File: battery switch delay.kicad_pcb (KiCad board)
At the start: 2 copper layers, 35.5 x 56 mm, 15 parts, among them J1 Conn_01x04, K2 G6E, Q1 2N3904, U2 LT1129-5.0_SOT223

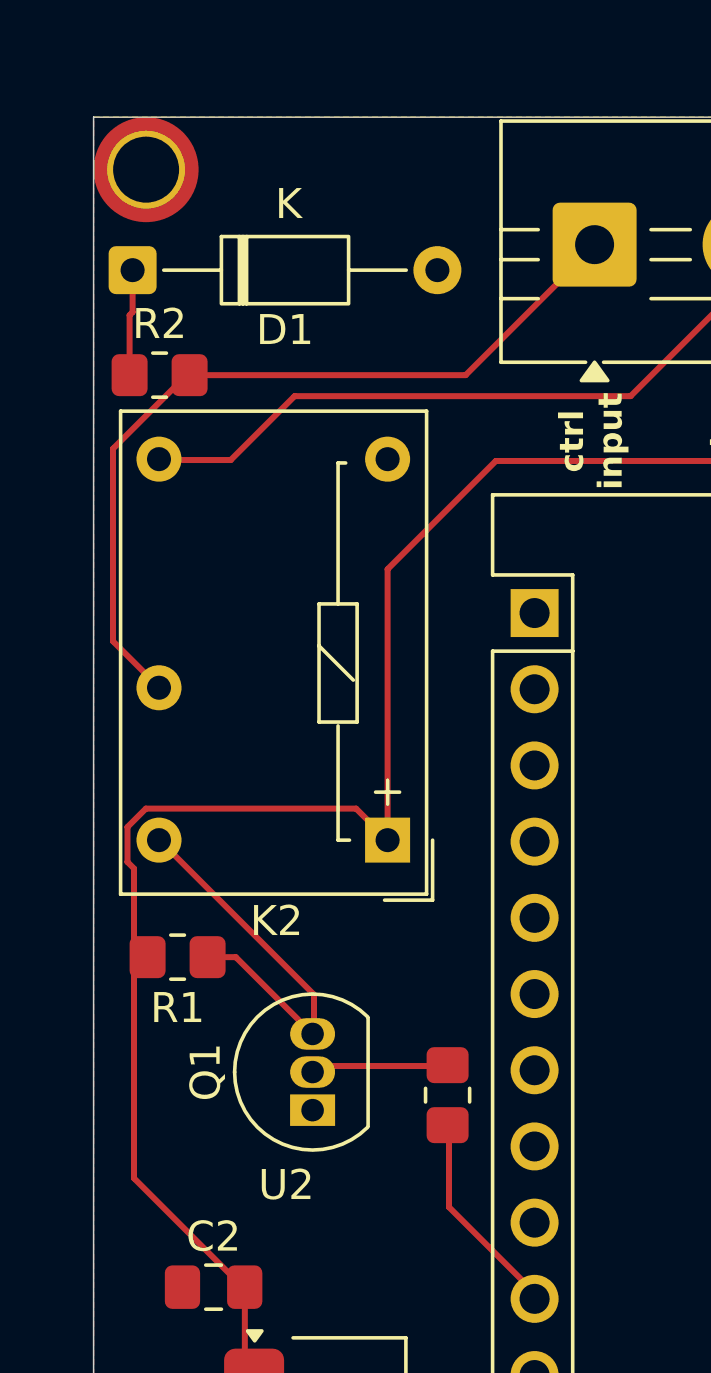
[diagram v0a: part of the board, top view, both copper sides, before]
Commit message: got the transistor the correct footprint hopefully
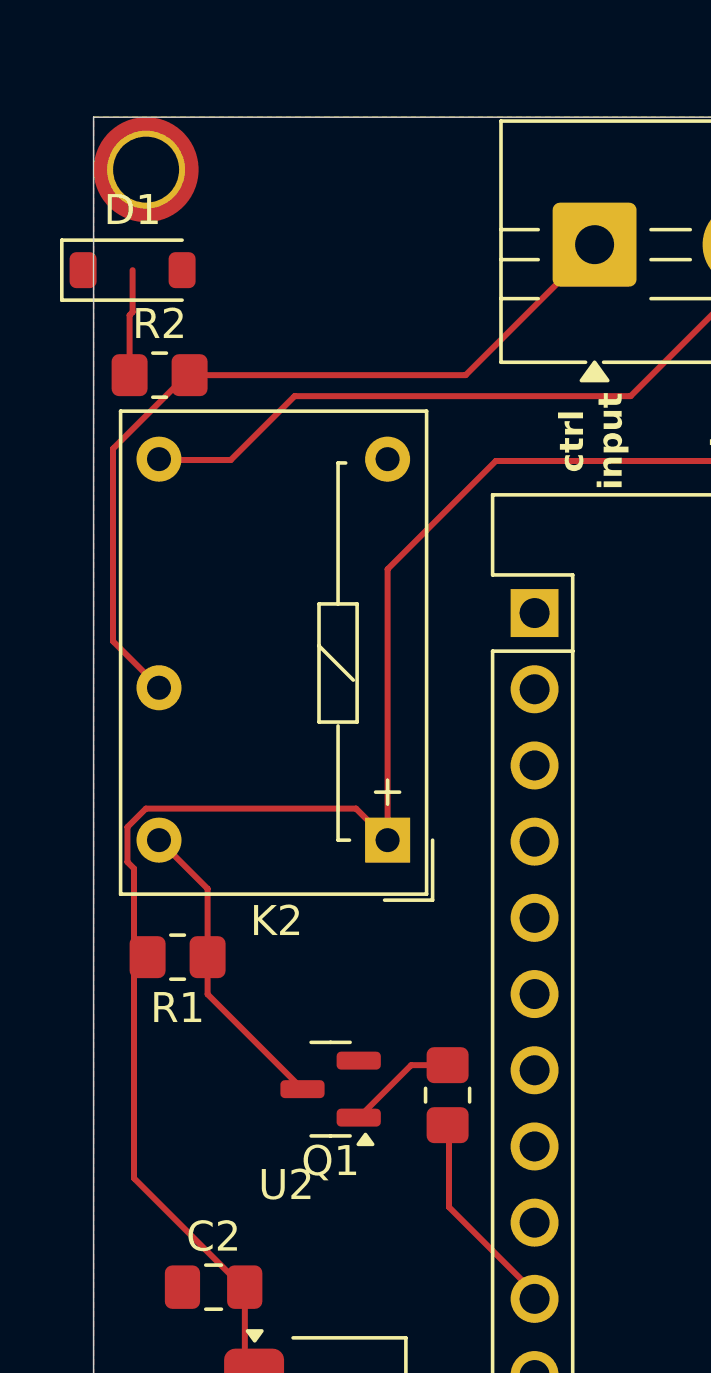
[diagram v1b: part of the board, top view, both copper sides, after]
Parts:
- D1: value ZPDxx -> 4.7v-5.1v zener diode; footprint Diode_THT:D_DO-35_SOD27_P10.16mm_Horizontal -> Diode_SMD:D_SOD-123
- J1: value Conn_01x04 -> 5mm pitch 4 position screw terminal block
- K2: value G6E -> G6E-134P-US
- Q1: value 2N3904 -> Q_NPN; footprint Package_TO_SOT_THT:TO-92_Inline -> Package_TO_SOT_SMD:SOT-23
- U2: value LT1129-5.0_SOT223 -> MIC2920A-12WS-TR_SOT223
- moved Q1 0.92 mm to (116.9, 88.9), turned to 180 degrees
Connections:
- Q1 pad 1: GND -> Net-(Q1-B)
- Q1 pad 2: Net-(Q1-B) -> GND
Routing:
- net Net-(Q1-C): track 13.2 -> 10.3 mm
- net Net-(Q1-B): track 5.14 -> 3.69 mm

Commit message: shuffling things around
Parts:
- moved D1 8.61 mm to (118.9, 61.3), turned to -90 degrees
- moved R3 5.56 mm to (118.0, 93.9), turned to 0 degrees
- moved R2 4.98 mm to (115.1, 62.0), turned to 90 degrees
- moved J1 1.00 mm to (126.7, 60.8)
- moved Q1 0.51 mm to (117.0, 88.4)
- moved R1 0.10 mm to (111.8, 84.6)
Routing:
- net ctrl: track 27.4 -> 30.0 mm
- net Net-(Q1-B): track 3.69 -> 5.52 mm
- net +12V: track 65.0 -> 66.7 mm
- net Net-(A1-D2): track 3.54 -> 5.06 mm
- net Net-(A1-D7): track 7.06 -> 5.60 mm
- net to switch: track 22.9 -> 23.5 mm

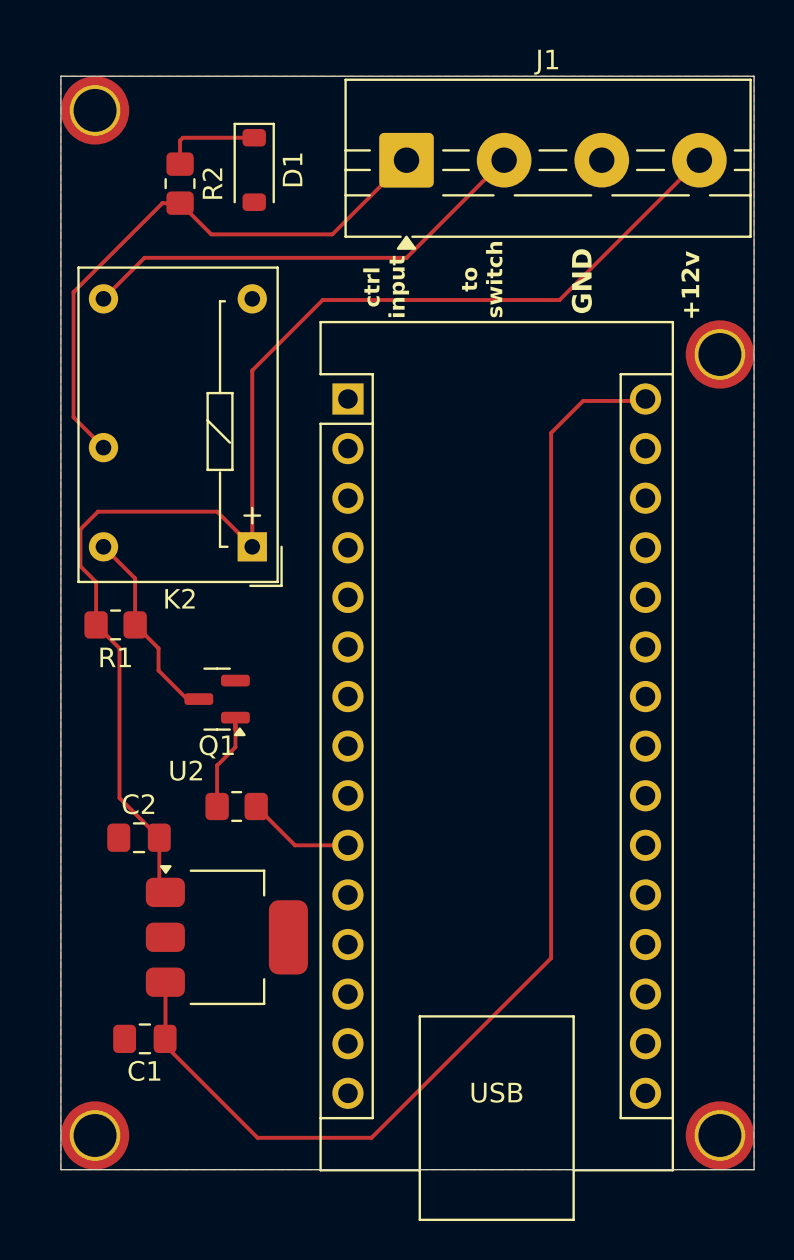
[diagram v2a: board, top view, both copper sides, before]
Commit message: did more board layout and actualy have all nets connected. looking at drc so i can be sure
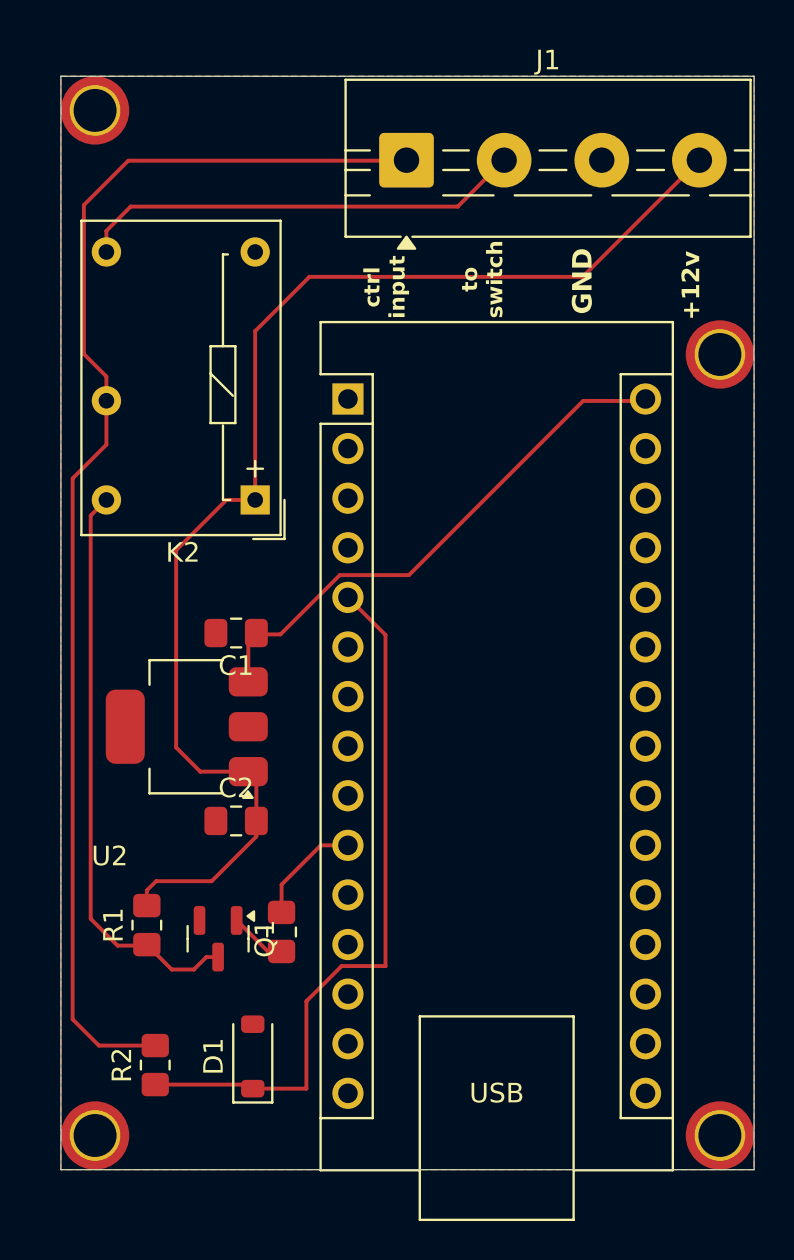
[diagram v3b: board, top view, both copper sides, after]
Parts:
- moved D1 45.4 mm to (118.8, 106.7), turned to 90 degrees
- moved R2 45.2 mm to (113.8, 107.1), turned to -90 degrees
- moved C1 21.3 mm to (118.0, 85.0)
- moved R1 15.5 mm to (113.4, 100.0), turned to -90 degrees
- moved Q1 12.3 mm to (117.0, 100.7), turned to -90 degrees
- moved U2 11.0 mm to (115.4, 89.8), turned to 180 degrees
- moved R3 6.82 mm to (120.3, 100.3), turned to 90 degrees
- moved C2 5.05 mm to (118.0, 94.6)
- moved K2 2.40 mm to (119.0, 78.2)
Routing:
- net ctrl: track 30.0 -> 65.2 mm
- net Net-(A1-VIN): track 61.4 -> 28.6 mm
- net Net-(A1-D2): track 5.06 -> 36.9 mm
- net Net-(Q1-C): track 10.2 -> 30.3 mm
- net Net-(Q1-B): track 5.52 -> 2.96 mm
- net +12V: track 66.7 -> 65.6 mm
- net Net-(A1-D7): track 5.60 -> 6.30 mm
- net to switch: track 23.5 -> 22.9 mm

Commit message: forgor to save lol
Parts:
- moved C1 10.9 mm to (114.2, 95.2), turned to 0 degrees
- moved C2 9.80 mm to (114.2, 85.6), turned to 180 degrees
- moved D1 1.42 mm to (117.4, 107.0), turned to -90 degrees
- moved U2 1.41 mm to (116.7, 90.4), turned to 0 degrees
- moved R2 0.98 mm to (113.3, 106.3), turned to 90 degrees
- moved R3 0.20 mm to (120.5, 100.5)
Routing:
- net Net-(A1-VIN): track 28.6 -> 41.0 mm
- net +12V: track 65.6 -> 61.9 mm
- net Net-(A1-D2): track 36.9 -> 33.4 mm
- net ctrl: track 65.2 -> 64.1 mm
- net Net-(Q1-C): track 30.3 -> 29.8 mm

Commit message: idk
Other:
- board text added: "https://github.com/titusmckay/pavati"
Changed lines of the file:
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@@
+		)
+	)
+	(gr_text "https://github.com/titusmckay/pavati"
+		(at 134.225 74.975 90)
+		(layer "B.SilkS")
+		(effects
+			(font
+				(size 1 1)
+				(thickness 0.1)
+			)
+			(justify left bottom mirror)
 		)
 	)

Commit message: more rand changes ig
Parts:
- C1: footprint Capacitor_SMD:C_0805_2012Metric_Pad1.18x1.45mm_HandSolder -> Capacitor_SMD:CP_Elec_4x5.4
- moved R1 3.43 mm to (113.3, 103.4)
- moved R2 3.22 mm to (115.6, 108.6)
- moved D1 3.13 mm to (119.7, 109.1)
- moved C1 3.07 mm to (115.7, 97.9)
- moved R3 2.95 mm to (120.4, 103.4)
- moved Q1 2.65 mm to (117.0, 103.3)
- moved C2 0.70 mm to (114.2, 84.9)
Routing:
- net +12V: track 61.9 -> 65.4 mm
- net ctrl: track 64.1 -> 67.3 mm
- net Net-(A1-D7): track 6.69 -> 8.77 mm
- net Net-(A1-VIN): track 41.0 -> 42.8 mm
- net Net-(Q1-C): track 29.8 -> 31.6 mm
- net Net-(A1-D2): track 33.4 -> 32.6 mm
